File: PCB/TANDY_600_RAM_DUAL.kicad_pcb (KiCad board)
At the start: 2 copper layers, 57.2 x 19.1 mm, 8 parts, among them CN1 TANDY_600_RAM_BUS_plain_pins, CN2 TANDY_600_RAM_BUS_plain_pins, U1 AS6C2008A, U2 HC148, U3 1G02

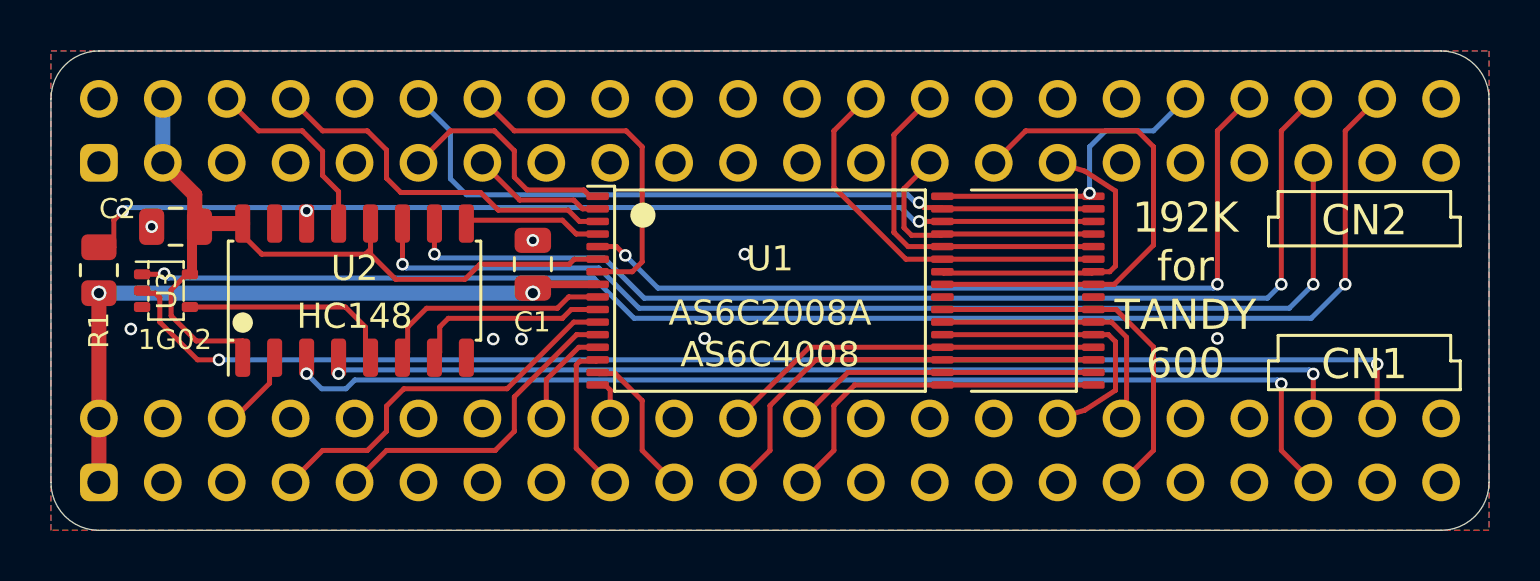
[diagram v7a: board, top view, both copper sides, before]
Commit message: footprints on dual
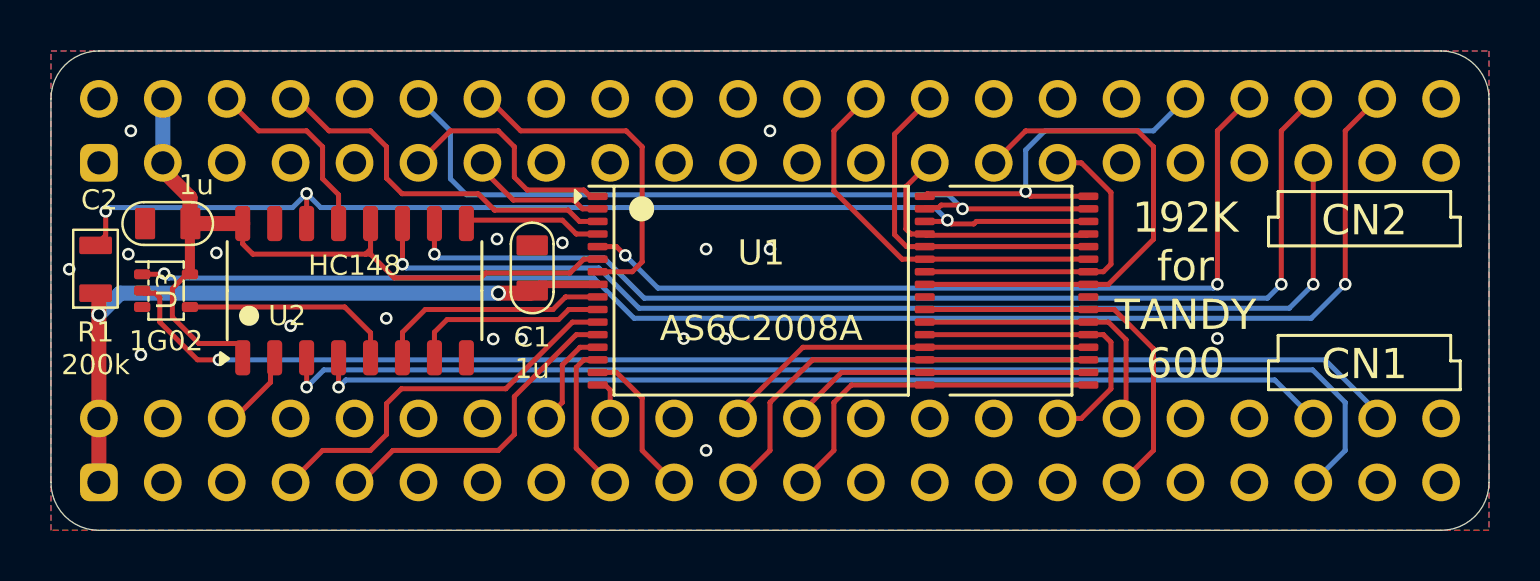
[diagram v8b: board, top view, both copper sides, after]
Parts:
- C1, C2: value 0.1u -> 1u
- moved U1 3.35 mm to (150.8, 109.2)
- moved C2 0.34 mm to (127.2, 106.6)
- moved C1 0.15 mm to (141.7, 108.3)
- moved R1 0.14 mm to (124.3, 108.4)
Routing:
- net /~{OE}: track 12.6 -> 15.5 mm
- net /~{B1_CS1_C}: track 44.3 -> 47.0 mm, vias 2 -> 1
- net /~{CE}: track 41.6 -> 43.5 mm
- net /A10: track 29.7 -> 31.2 mm
- net /B1_CS2: track 53.0 -> 51.9 mm, vias 2 -> 1
- net /D1: track 14.9 -> 15.6 mm
- net /D0: track 10.9 -> 11.5 mm
- net /~{B1_CS1_B}: track 41.3 -> 40.7 mm, vias 2 -> 1
- net /D4: track 20.1 -> 20.6 mm
- net GND: vias 8 -> 18
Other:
- board text removed: "C1,C2: ${6abd93ae-8309-4193-b5c6-e97f8e789dbe:VALUE} R1: ${0c359dbe-85cf-44c5-9fd0-3b040d8e3d19:VALUE}"
